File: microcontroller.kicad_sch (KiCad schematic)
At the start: 24 parts, among them U1 MIMXRT1062DVJ6B, Y1 32.768kHz

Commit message: schematic update
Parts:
- removed C17, C21, C23, C25, C28, C30: 0.22uf, Capacitor_SMD:C_0603_1608Metric, symbol Device:C
- removed C18, C26, C29: 10uf, Capacitor_SMD:C_0805_2012Metric, symbol Device:C
- removed C19, C22, C24, C27: 4.7uf, Capacitor_SMD:C_0603_1608Metric, symbol Device:C
- removed C20: 10nf, Capacitor_SMD:C_0603_1608Metric, symbol Device:C
- removed FB1: Ferrite_Bead, Resistor_SMD:R_0805_2012Metric, symbol Device:Ferrite_Bead
- removed L2: 4.7uH, Capacitor_SMD:C_0805_2012Metric, symbol Device:L
- removed R30: 1k, Resistor_SMD:R_0402_1005Metric, symbol Device:R
- removed TP1, TP2: TestPoint, TestPoint:TestPoint_Pad_D1.0mm, symbol Connector:TestPoint
- removed U1: MIMXRT1062DVJ6B, MIMXRT1062DVJ6B:BGA196C80P14X14_1200X1200X152N, symbol adcs:MIMXRT1062DVJ6B
- added C10, C11: 22uF, Capacitor_SMD:C_0603_1608Metric, symbol mainboard:22UF-0805-6.3V-20%
- added C12, C13: 100uF, Capacitor_SMD:C_1210_3225Metric, symbol mainboard:22UF-1210-16V-20%
- added C14: 0.1uF, Capacitor_SMD:C_0603_1608Metric, symbol mainboard:1.0UF-0603-16V-10%
- added C15: 3.3nF, Capacitor_SMD:C_0603_1608Metric, symbol mainboard:3.3NF-0603-100V-10%
- added C16: 1uF, Capacitor_SMD:C_0603_1608Metric, symbol mainboard:1.0UF-0603-16V-10%
- added C17, C20, C25, C28, C51: 4.7uF, symbol pycubed_mainboard:10NF_10000PF-50V-10%(0603)
- added C18, C21, C23, C26, C27, C29, C52, C59: 0.22uF, symbol pycubed_mainboard:10NF_10000PF-50V-10%(0603)
- added C19, C22, C31, C50: 10uF, symbol pycubed_mainboard:10NF_10000PF-50V-10%(0603)
- added C24: 2.2uF, symbol pycubed_mainboard:10NF_10000PF-50V-10%(0603)
- added C31: 10nF, symbol pycubed_mainboard:10NF_10000PF-50V-10%(0603)
- added C32: 4.7uF, Capacitor_SMD:C_0603_1608Metric, symbol Device:C_Small
- added C47, C48: 10pF, Capacitor_SMD:C_0603_1608Metric, symbol mainboard:C_Small
- added C49: 0.1uF, Capacitor_SMD:C_0603_1608Metric, symbol mainboard:C_Small
- added D2: LED, LED_SMD:LED_0402_1005Metric, symbol Device:LED
- added D3: SP0503BAHT, Package_TO_SOT_SMD:SOT-143, symbol Power_Protection:SP0503BAHT
- added D4: CDBA240LL-HF, sapling:DO-214AC, symbol Device:D_Schottky
- added F1: Fuse, symbol Device:Fuse
- added FB1, FB2: FerriteBead, symbol Device:FerriteBead
- added IC1: MIMXRT1062DVJ6B, BGA196C80P14X14_1200X1200X152, symbol adcs:MIMXRT1062DVJ6B
- added J10: JTAG_SWD_10, Connector_PinHeader_1.27mm:PinHeader_2x05_P1.27mm_Vertical_SMD, symbol Connector:Conn_ARM_JTAG_SWD_10
- added J3: 503182-1852, mainboard:MOLEX_503182-1852, symbol mainboard:503182-1852
- added J4: USB_C_pycubed, mainboard:USB_C_Receptacle_XKB_U262-161N-4BVC11, symbol mainboard:USB_C_pycubed
- added J6: Conn_01x06, Connector_PinHeader_2.54mm:PinHeader_1x06_P2.54mm_Vertical, symbol Connector_Generic:Conn_01x06
- added L1: 3.3uH, mainboard:L_2141, symbol Device:L
- added L3: 4.7uH, symbol pycubed_mainboard:Device_L
- added Q6: DMG2305UX-7, DMG2305UX-7:SOT91P240X110-3N_DMG2305UX-7, symbol adcs:DMG2305UX-7
- added R20: 1k, symbol pycubed_mainboard:RESISTOR0603
- added R27: 73.2K, Resistor_SMD:R_0603_1608Metric, symbol mainboard:R-US_R0603
- added R28: 22.1K, Resistor_SMD:R_0603_1608Metric, symbol mainboard:R-US_R0603
- added R29 (x2): 100K, Resistor_SMD:R_0603_1608Metric, symbol mainboard:R-US_R0603
- added R37: 100k, Resistor_SMD:R_0603_1608Metric, symbol Device:R_US
- added R37, R38: 10k, Resistor_SMD:R_0603_1608Metric, symbol Device:R_US
- added R37: 1k, Resistor_SMD:R_0603_1608Metric, symbol Device:R_US
- added R39, R40: 5.1k, Resistor_SMD:R_0603_1608Metric, symbol Device:R_US
- added SW1: KMR231NG LFS, mainboard:BTN_KMR2_4.6X2.8, symbol mainboard:SWITCH_SMT4.6X2.8
- added U6: TPS54226PWPR, mainboard:PWP14_2P31X2P46-L, symbol mainboard:TPS54226PWPRPWP14_2P31X2P46-L
- added U7: MR25H40MDF, mainboard:SON127P600X500X90-9N, symbol mainboard:MR25H40MDF
- added U8: MKL02Z32VFG4, Package_DFN_QFN:QFN-16-1EP_3x3mm_P0.5mm_EP1.8x1.8mm, symbol adcs:MKL02Z32VFG4
- added Y2: 32.768kHz, Crystal:Crystal_SMD_3215-2Pin_3.2x1.5mm, symbol Device:Crystal
- C8, C9: value 8pF -> 10pF
- Y1: value 32.768kHz -> 24.0mHz; footprint Crystal:Crystal_SMD_3215-2Pin_3.2x1.5mm -> Crystal:Crystal_SMD_2016-4Pin_2.0x1.6mm; Flight ABS07-32.768KHZ-T -> XRCGB24M000F1SBDR0; Manufacturer_Name Abracon LLC -> Murata Electronics; Manufacturer_Part_Number SC-32S32.768kHz20PPM7pF -> XRCGB24M000F1SBDR0; Proto SC-32S32.768kHz20PPM7pF -> (none)
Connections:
- net FLASH.IO0: now also IC1.P3 (GPIO_SD_B1_08), U7.3 (~{WP})
- net FLASH.IO2: now also IC1.N4 (GPIO_SD_B1_09), U7.5 (SI)
- net FLASH.IO3: now also IC1.L3 (GPIO_SD_B1_06), U7.1 (~{CS})
- net FLASH.SCK: now also IC1.L4 (GPIO_SD_B1_07), U7.2 (SO)
- net GND: now also C10.1, C11.1, C12.2, C13.2, C15.2, C16.2, C17.2, C18.2, C19.2, C20.2, C21.2, C22.2, C23.2, C24.2, C25.2, C26.2, C27.2, C28.2, C29.2, C31.2, C31.2, C47.2, C48.2, C49.2, C50.2, C51.2, C52.2, C59.2, IC1.A1 (VSS_1), IC1.A14 (VSS_2), IC1.B10 (VSS_4), IC1.B5 (VSS_3), IC1.E13 (VSS_6), IC1.E2 (VSS_5), IC1.G14 (GPIO_AD_B0_05), IC1.G7 (VSS_7), IC1.G8 (VSS_8), IC1.H7 (VSS_9), IC1.H8 (VSS_10), IC1.J7 (VSS_11), IC1.J8 (VSS_12), IC1.K13 (VSS_14), IC1.K2 (VSS_13), IC1.K9 (NGND_KEL0), IC1.L9 (VSS_15), IC1.N1 (DCDC_GND_1), IC1.N2 (DCDC_GND_2), IC1.N5 (VSS_16), IC1.N8 (VSS_17), IC1.P1 (VSS_18), IC1.P14 (VSS_19), J10.3 (GND), J10.5 (GND), J10.9 (GNDDetect), J3.6 (VSS), J3.P1 (SHIELD), J3.P2 (SHIELD), J3.P3 (SHIELD), J3.P4 (SHIELD), J3.P5 (SHIELD), J6.5 (Pin_5), Q6.1, R28.1, R37.1, SW1.B (S), SW1.B' (S1), U6.15 (EPAD), U6.5 (GND), U6.8 (PGND1), U6.9 (PGND2), U7.4 (VSS), U7.9 (EP), U8.17 (EPAD), U8.2 (VSS)
- net SD.CLK: now also IC1.J3 (GPIO_SD_B0_01), J3.5 (CLK)
- net SD.CMD: now also IC1.J4 (GPIO_SD_B0_00), J3.3 (CMD)
- net SD.DAT0: now also IC1.J1 (GPIO_SD_B0_02), J3.7 (DAT0)
- net SD.DAT1: now also IC1.K1 (GPIO_SD_B0_03), J3.8 (DAT1)
- net SD.DAT2: now also IC1.H2 (GPIO_SD_B0_04), J3.1 (DATA2)
- net SD.DAT3: now also IC1.J2 (GPIO_SD_B0_05), J3.2 (CD/DAT3), R38.1
- net at C8.1, Y1.1: now also IC1.N9 (RTC_XTALI)
- net at C9.1, Y1.2: now also IC1.P9 (RTC_XTALO)
- net at D1.2 (A): now also R20.2
- new net: C14.1, L1.1, U6.10 (SW1), U6.11 (SW2)
- new net: C25.1, C27.1, IC1.P10 (NVCC_PLL)
- new net: C14.2, U6.12 (VBST)
- new net: R27.1, R28.2, U6.2 (VFB)
- new net: C16.1, R29.2, U6.3 (VREG5)
- new net: C15.1, U6.4 (SS)
- new net: R29.1, U6.6 (PG)
- new net: IC1.K7 (PMIC_ON_REQ), R29.1, U6.7 (EN)
- new net: C47.1, IC1.P11 (XTALI), Y2.1
- new net: C20.1, C21.1, C22.1, C23.1, C24.1, IC1.E9 (NVCC_GPIO_1), IC1.F10 (NVCC_GPIO_2), IC1.F4 (GPIO_EMC_02), IC1.F5 (NVCC_EMC_2), IC1.J10 (NVCC_GPIO_3), IC1.J6 (NVCC_SD0), IC1.K4 (DCDC__IN_Q), IC1.K5 (NVCC_SD1), IC1.N14 (VDDA_ADC_3P3), IC1.P12 (VDD_HIGH_IN)
- new net: FB1.2, Q6.3
- new net: F1.2, FB1.1
- new net: C31.1, C50.1, C51.1, C52.1, IC1.F6 (VDD_SOC_IN_1), IC1.F7 (VDD_SOC_IN_2), IC1.F8 (VDD_SOC_IN_3), IC1.F9 (VDD_SOC_IN_4), IC1.G6 (VDD_SOC_IN_5), IC1.G9 (VDD_SOC_IN_6), IC1.H6 (VDD_SOC_IN_7), IC1.H9 (VDD_SOC_IN_8), IC1.J5 (DCDC_SENSE), IC1.J9 (VDD_SOC_IN_9), L3.1
- new net: C48.1, IC1.N11 (XTALO), Y2.2
- new net: C31.1, C59.1, D4.2 (A), IC1.K8 (VDD_USB_CAP)
- new net: IC1.M1 (DCDC_LP_1), IC1.M2 (DCDC_LP_2), L3.2
- new net: C28.1, C29.1, IC1.P8 (VDD_HIGH_CAP)
- new net: C17.1, C18.1, C19.1, FB2.2, IC1.L1 (DCDC_IN_1), IC1.L2 (DCDC_IN_2)
- new net: C26.1, IC1.M10 (VDD_SNVS_CAP)
- new net: IC1.D8 (GPIO_B0_03), R20.1
- new net: IC1.D10 (GPIO_B0_13), U8.12 (PTB4)
- new net: IC1.F11 (GPIO_AD_B0_04), U8.4 (PTA4)
- new net: IC1.F3 (GPIO_EMC_01), U8.15 (PTA1)
- new net: D4.1 (K), IC1.M9 (VDD_SNVS_IN)
- new net: IC1.P4 (GPIO_SD_B1_10), U7.6 (SCK)
- new net: D2.1 (K), R37.2
- new net: R37.1, U8.11 (PTB3)
- new net +3V3: C10.2, C11.2, D2.2 (A), FB2.1, J10.1 (VTref), L1.2, R27.2, R29.2, U6.1 (VO), U8.1 (VDD)
- new net +5V: IC1.N6 (USB_OTG1_VBUS), IC1.P6 (USB_OTG2_VBUS), J6.1 (Pin_1), Q6.2
- new net +5VD: C32.2, D3.2 (K), F1.1, J4.A4 (VBUS), J4.A9 (VBUS)
- new net 3.3V: C49.1, J3.4 (VDD), R37.2, R38.2, U7.8 (VDD)
- new net FLASH.CS: IC1.P5 (GPIO_SD_B1_11), U7.7 (~{HOLD})
- new net GNDREF: C32.1, D3.1 (A), J4.A1 (GND), J4.A12 (GND), J4.S1 (SHIELD), J6.6 (Pin_6), R39.1, R40.1
- new net GPIO_AD_B0_02: IC1.M11 (GPIO_AD_B0_02)
- new net GPIO_AD_B0_03: IC1.G11 (GPIO_AD_B0_03), IC1.J14 (GPIO_AD_B1_15)
- new net GPIO_AD_B0_12: IC1.K14 (GPIO_AD_B0_12)
- new net GPIO_AD_B0_13: IC1.L14 (GPIO_AD_B0_13)
- new net GPIO_AD_B1_00: IC1.J11 (GPIO_AD_B1_00)
- new net GPIO_AD_B1_01: IC1.K11 (GPIO_AD_B1_01)
- new net GPIO_AD_B1_02: IC1.L11 (GPIO_AD_B1_02)
- new net GPIO_AD_B1_03: IC1.M12 (GPIO_AD_B1_03)
- new net GPIO_AD_B1_04: IC1.L12 (GPIO_AD_B1_04)
- new net GPIO_AD_B1_05: IC1.K12 (GPIO_AD_B1_05), IC1.M14 (GPIO_AD_B0_00)
- new net GPIO_AD_B1_06: IC1.J12 (GPIO_AD_B1_06)
- new net GPIO_AD_B1_07: IC1.K10 (GPIO_AD_B1_07)
- new net GPIO_AD_B1_08: IC1.H13 (GPIO_AD_B1_08)
- new net GPIO_AD_B1_09: IC1.M13 (GPIO_AD_B1_09)
- new net GPIO_AD_B1_10: IC1.L13 (GPIO_AD_B1_10)
- new net GPIO_AD_B1_11: IC1.J13 (GPIO_AD_B1_11)
- new net GPIO_AD_B1_12: IC1.H12 (GPIO_AD_B1_12)
- new net GPIO_AD_B1_13: IC1.H11 (GPIO_AD_B1_13)
- new net GPIO_AD_B1_14: IC1.G12 (GPIO_AD_B1_14)
- new net GPIO_B0_00: IC1.D7 (GPIO_B0_00)
- new net GPIO_B0_01: IC1.E7 (GPIO_B0_01)
- new net GPIO_B0_02: IC1.E8 (GPIO_B0_02)
- new net GPIO_B0_10: IC1.D9 (GPIO_B0_10)
- new net GPIO_B0_11: IC1.A10 (GPIO_B0_11)
- new net GPIO_B0_12: IC1.C10 (GPIO_B0_12)
- new net GPIO_B0_14: IC1.E10 (GPIO_B0_14)
- new net GPIO_B1_00: IC1.A11 (GPIO_B1_00)
- new net GPIO_B1_01: IC1.B11 (GPIO_B1_01)
- new net GPIO_B1_02: IC1.C11 (GPIO_B1_02)
- new net GPIO_B1_03: IC1.D11 (GPIO_B1_03)
- new net GPIO_B1_04: IC1.E12 (GPIO_B1_04)
- new net GPIO_B1_05: IC1.D12 (GPIO_B1_05)
- new net GPIO_B1_06: IC1.C12 (GPIO_B1_06)
- new net GPIO_B1_07: IC1.B12 (GPIO_B1_07)
- new net GPIO_B1_08: IC1.A12 (GPIO_B1_08)
- new net GPIO_B1_10: IC1.B13 (GPIO_B1_10)
- new net GPIO_B1_11: IC1.C13 (GPIO_B1_11)
- new net GPIO_B1_12: IC1.D13 (GPIO_B1_12)
- new net GPIO_B1_13: IC1.D14 (GPIO_B1_13)
- new net GPIO_B1_14: IC1.C14 (GPIO_B1_14)
- new net GPIO_B1_15: IC1.B14 (GPIO_B1_15), IC1.E11 (GPIO_B0_15)
- new net GPIO_EMC_04: IC1.F2 (GPIO_EMC_04)
- new net GPIO_EMC_05: IC1.G5 (GPIO_EMC_05)
- new net GPIO_EMC_06: IC1.H5 (GPIO_EMC_06)
- new net GPIO_EMC_07: IC1.H4 (GPIO_EMC_07)
- new net GPIO_EMC_08: IC1.H3 (GPIO_EMC_08)
- new net GPIO_EMC_31: IC1.C5 (GPIO_EMC_31)
- new net GPIO_EMC_32: IC1.D5 (GPIO_EMC_32)
- new net GPIO_EMC_36: IC1.C3 (GPIO_EMC_36)
- new net GPIO_EMC_37: IC1.E4 (GPIO_EMC_37)
- new net JTAG.MUX.MOD: IC1.F13 (GPIO_AD_B0_08), U8.13 (PTB5)
- new net JTAG.MUX.TCK: IC1.F12 (GPIO_AD_B0_07), J10.4 (SWDCLK/TCK), U8.8 (PTB0)
- new net JTAG.MUX.TDI: IC1.F14 (GPIO_AD_B0_09), J10.8 (NC/TDI), U8.7 (PTA7)
- new net JTAG.MUX.TDO: IC1.G13 (GPIO_AD_B0_10), J10.6 (SWO/TDO), U8.6 (PTA6)
- new net JTAG.MUX.TMS: IC1.E14 (GPIO_AD_B0_06), J10.2 (SWDIO/TMS), U8.5 (PTA5)
- new net JTAG.MUX.TRSTB: IC1.G10 (GPIO_AD_B0_11), IC1.K3 (DCDC_PSWITCH), J10.10 (~{RESET}), R37.2, U8.3 (PTA3)
- new net ONOFF: IC1.M6 (ONOFF)
- new net POR_B: IC1.M7 (POR_B), U8.9 (PTB1)
- new net PROG: SW1.A (P), SW1.A' (P1), U8.10 (PTB2)
- new net USB1_CC1: J4.A5 (CC1), R40.2
- new net USB1_CC2: J4.B5 (CC2), R39.2
- new net USB1_D+: D3.4 (K), IC1.L8 (USB_OTG1_DP), J4.A6 (D+), J4.B6 (D+)
- new net USB1_D-: D3.3 (K), IC1.M8 (USB_OTG1_DN), J4.A7 (D-), J4.B7 (D-)
- new net VADCS_IN: C12.1, C13.1, J6.2 (Pin_2), U6.13 (VIN), U6.14 (VCC)
- new net WAKEUP: IC1.L6 (WAKEUP)
- no-connect marks 0 -> 14
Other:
- note added: ""GND""
- note added: ""VUSB""
- note added: ""XXX""
- note added: "3.3V Regulator"
- note added: "Add jumper to allow USB battery charging (even inside deployer)."
- note added: "Double check component choice"
- note added: "Figure out where to put C8"
- note added: "MRAM - Nonvolatile Memory (4MB)"
- note added: "MicroSD Card"
- note added: "Populate (and program) with either MKL02 from PJRC pre-programmed with the Teensy Bootloader; or with JTAG/SWD connector"
- note added: "Programmer"
- note added: "RBF Jumpers"
- note added: "Remove both jumpers before flight"
- note added: "Should these be grounded or disconnected?"
- note added: "USB-C"
- note added: "VBATT 4.5 to 18V"
- note added: "pull up on CS?"
- note removed: "RT1062"
- note removed: "TODO: add 24khz crystal here"

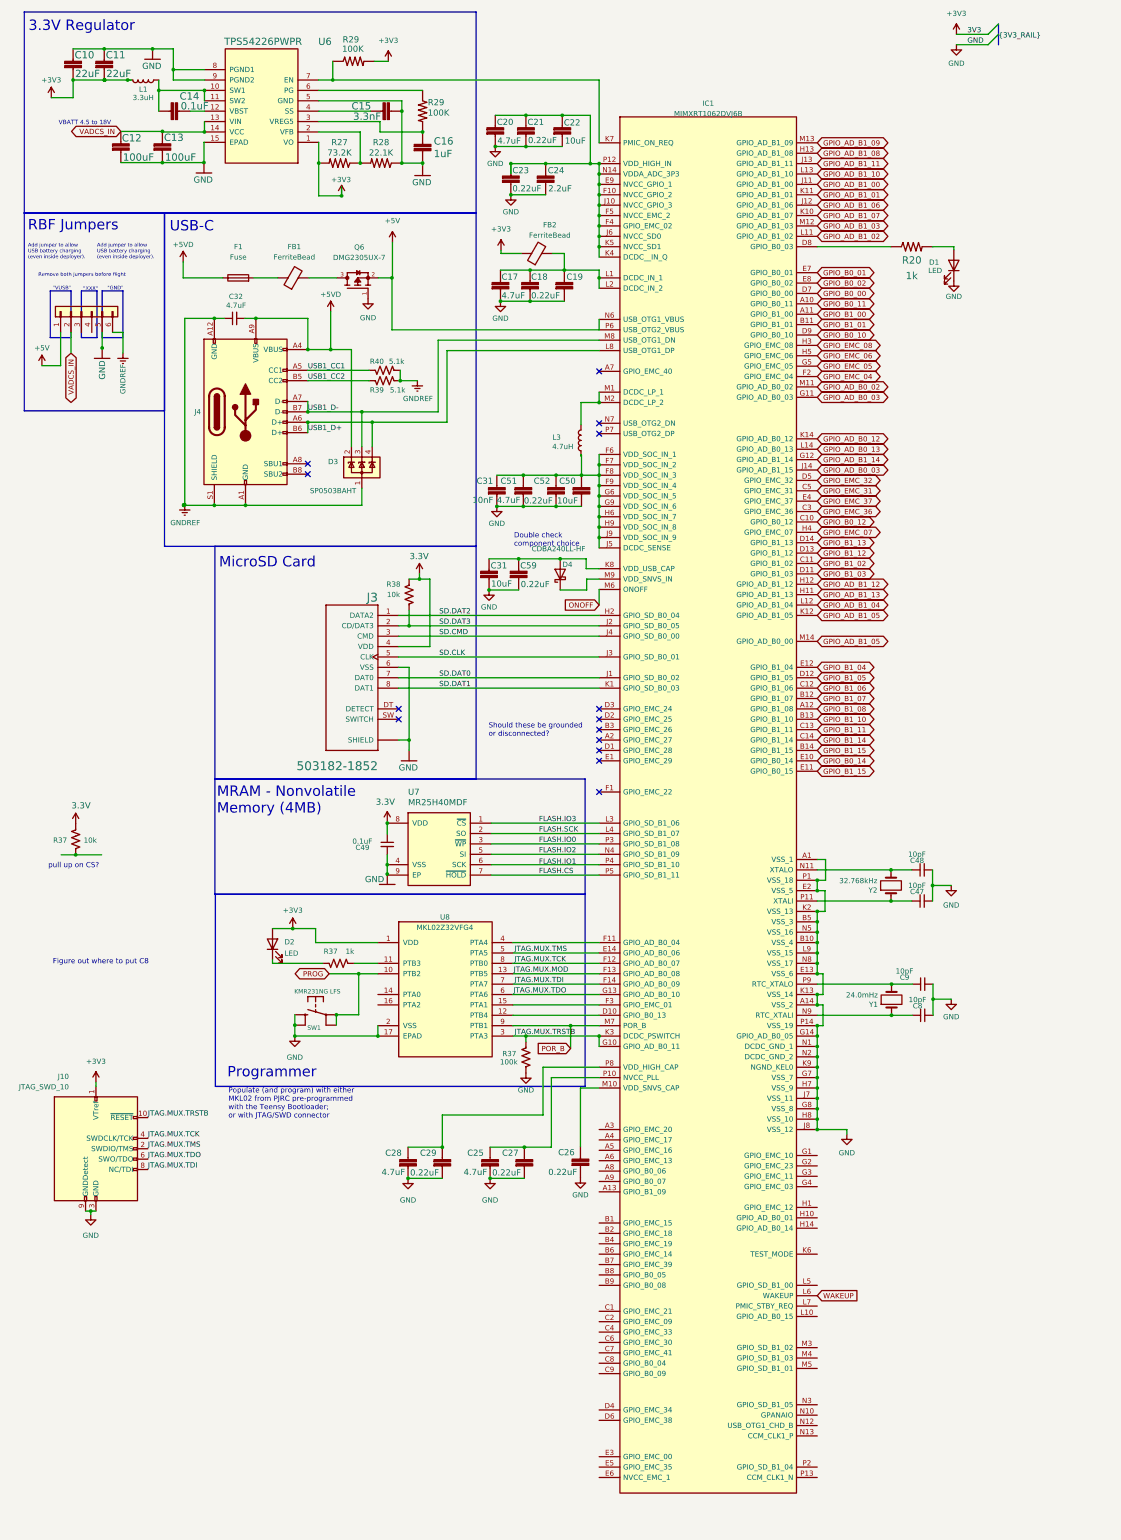
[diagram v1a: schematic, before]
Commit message: update schematic
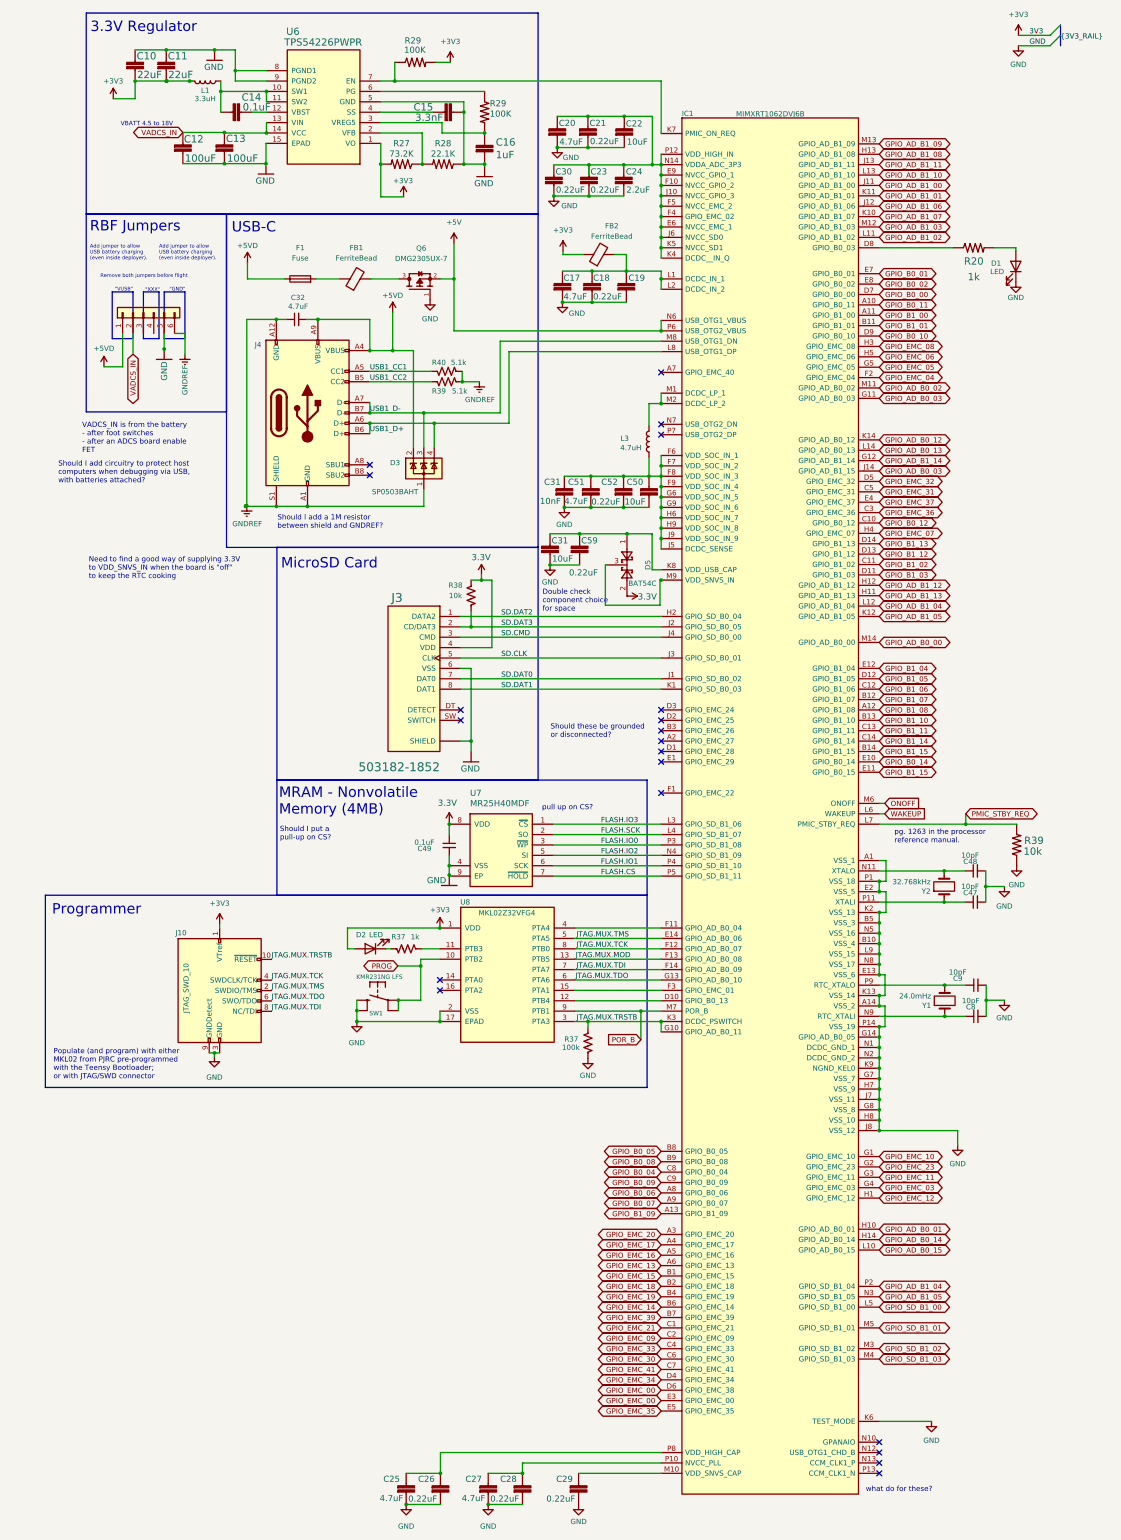
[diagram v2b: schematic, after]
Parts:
- removed D4: CDBA240LL-HF, sapling:DO-214AC, symbol Device:D_Schottky
- removed R37: 10k, Resistor_SMD:R_0603_1608Metric, symbol Device:R_US
- added C30: 0.22uF, symbol pycubed_mainboard:10NF_10000PF-50V-10%(0603)
- added D5: BAT54C, Package_TO_SOT_SMD:SOT-23, symbol Diode:BAT54C
- added R39: 10k, symbol pycubed_mainboard:RESISTOR0603
- C27: value 0.22uF -> 4.7uF
- C28: value 4.7uF -> 0.22uF
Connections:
- net +5V: no longer J6.1 (Pin_1)
- net +5VD: now also J6.1 (Pin_1)
- net 3.3V: now also D5.2
- net FLASH.IO1: now also IC1.P4 (GPIO_SD_B1_10), U7.6 (SCK)
- net GND: now also IC1.K6 (TEST_MODE), C30.2, R39.1
- net GPIO_AD_B1_04: now also IC1.P2 (GPIO_SD_B1_04)
- net GPIO_AD_B1_05: now also IC1.N3 (GPIO_SD_B1_05); no longer IC1.M14 (GPIO_AD_B0_00)
- net at C27.1, IC1.P10 (NVCC_PLL): now also C28.1; no longer C25.1
- net at C20.1, C21.1, C22.1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: now also IC1.E6 (NVCC_EMC_1), C30.1
- net at C31.1, C59.1, IC1.K8 (VDD_USB_CAP): now also D5.1
- net at C26.1: now also C25.1, IC1.P8 (VDD_HIGH_CAP); no longer IC1.M10 (VDD_SNVS_CAP)
- net GPIO_B1_09: now reaches IC1.A13 (GPIO_B1_09)
- net GPIO_EMC_20: now reaches IC1.A3 (GPIO_EMC_20)
- net GPIO_EMC_17: now reaches IC1.A4 (GPIO_EMC_17)
- net GPIO_EMC_16: now reaches IC1.A5 (GPIO_EMC_16)
- net GPIO_EMC_13: now reaches IC1.A6 (GPIO_EMC_13)
- net GPIO_B0_06: now reaches IC1.A8 (GPIO_B0_06)
- net GPIO_B0_07: now reaches IC1.A9 (GPIO_B0_07)
- net GPIO_EMC_15: now reaches IC1.B1 (GPIO_EMC_15)
- net GPIO_EMC_18: now reaches IC1.B2 (GPIO_EMC_18)
- net GPIO_EMC_19: now reaches IC1.B4 (GPIO_EMC_19)
- net GPIO_EMC_14: now reaches IC1.B6 (GPIO_EMC_14)
- net GPIO_EMC_39: now reaches IC1.B7 (GPIO_EMC_39)
- net GPIO_B0_05: now reaches IC1.B8 (GPIO_B0_05)
- net GPIO_B0_08: now reaches IC1.B9 (GPIO_B0_08)
- net GPIO_EMC_21: now reaches IC1.C1 (GPIO_EMC_21)
- net GPIO_EMC_09: now reaches IC1.C2 (GPIO_EMC_09)
- net GPIO_EMC_33: now reaches IC1.C4 (GPIO_EMC_33)
- net GPIO_EMC_30: now reaches IC1.C6 (GPIO_EMC_30)
- net GPIO_EMC_41: now reaches IC1.C7 (GPIO_EMC_41)
- net GPIO_B0_04: now reaches IC1.C8 (GPIO_B0_04)
- net GPIO_B0_09: now reaches IC1.C9 (GPIO_B0_09)
- net GPIO_EMC_34: now reaches IC1.D4 (GPIO_EMC_34)
- net GPIO_EMC_00: now reaches IC1.D6 (GPIO_EMC_38)
- net GPIO_EMC_00: now also IC1.E3 (GPIO_EMC_00)
- net GPIO_EMC_35: now reaches IC1.E5 (GPIO_EMC_35)
- net GPIO_EMC_10: now reaches IC1.G1 (GPIO_EMC_10)
- net GPIO_EMC_23: now reaches IC1.G2 (GPIO_EMC_23)
- net GPIO_EMC_11: now reaches IC1.G3 (GPIO_EMC_11)
- net GPIO_EMC_03: now reaches IC1.G4 (GPIO_EMC_03)
- net GPIO_EMC_12: now reaches IC1.H1 (GPIO_EMC_12)
- net GPIO_AD_B0_01: now reaches IC1.H10 (GPIO_AD_B0_01)
- net GPIO_AD_B0_14: now reaches IC1.H14 (GPIO_AD_B0_14)
- net GPIO_AD_B0_15: now reaches IC1.L10 (GPIO_AD_B0_15)
- net GPIO_SD_B1_00: now reaches IC1.L5 (GPIO_SD_B1_00)
- net PMIC_STBY_REQ: now reaches IC1.L7 (PMIC_STBY_REQ)
- net PMIC_STBY_REQ: now also R39.2
- net GPIO_SD_B1_02: now reaches IC1.M3 (GPIO_SD_B1_02)
- net GPIO_SD_B1_03: now reaches IC1.M4 (GPIO_SD_B1_03)
- net GPIO_SD_B1_01: now reaches IC1.M5 (GPIO_SD_B1_01)
- net at IC1.M9 (VDD_SNVS_IN): now also D5.3
- new net: C29.1, IC1.M10 (VDD_SNVS_CAP)
- new net GPIO_AD_B0_00: IC1.M14 (GPIO_AD_B0_00)
- no-connect marks 14 -> 20
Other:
- note added: "Double check component choice for space"
- note added: "Need to find a good way of supplying 3.3V to VDD_SNVS_IN when the board is "off" to keep the RTC cooking"
- note added: "Should I add a 1M resistor between shield and GNDREF?"
- note added: "Should I add circuitry to protect host computers when debugging via USB, with batteries attached?"
- note added: "Should I put a pull-up on CS?"
- note added: "VADCS_IN is from the battery - after foot switches - after an ADCS board enable FET"
- note added: "pg. 1263 in the processor reference manual."
- note added: "what do for these?"
- note removed: "Double check component choice"
- note removed: "Figure out where to put C8"
- moved on the sheet: C10, C11, C12, C13, C14, C15, C16, C17, C18, C19, C20, C21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
